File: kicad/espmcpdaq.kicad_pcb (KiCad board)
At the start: 2 copper layers, 151.1 x 149.9 mm, 31 parts, among them J2 Conn_01x15_Female, J3 Conn_01x15_Female

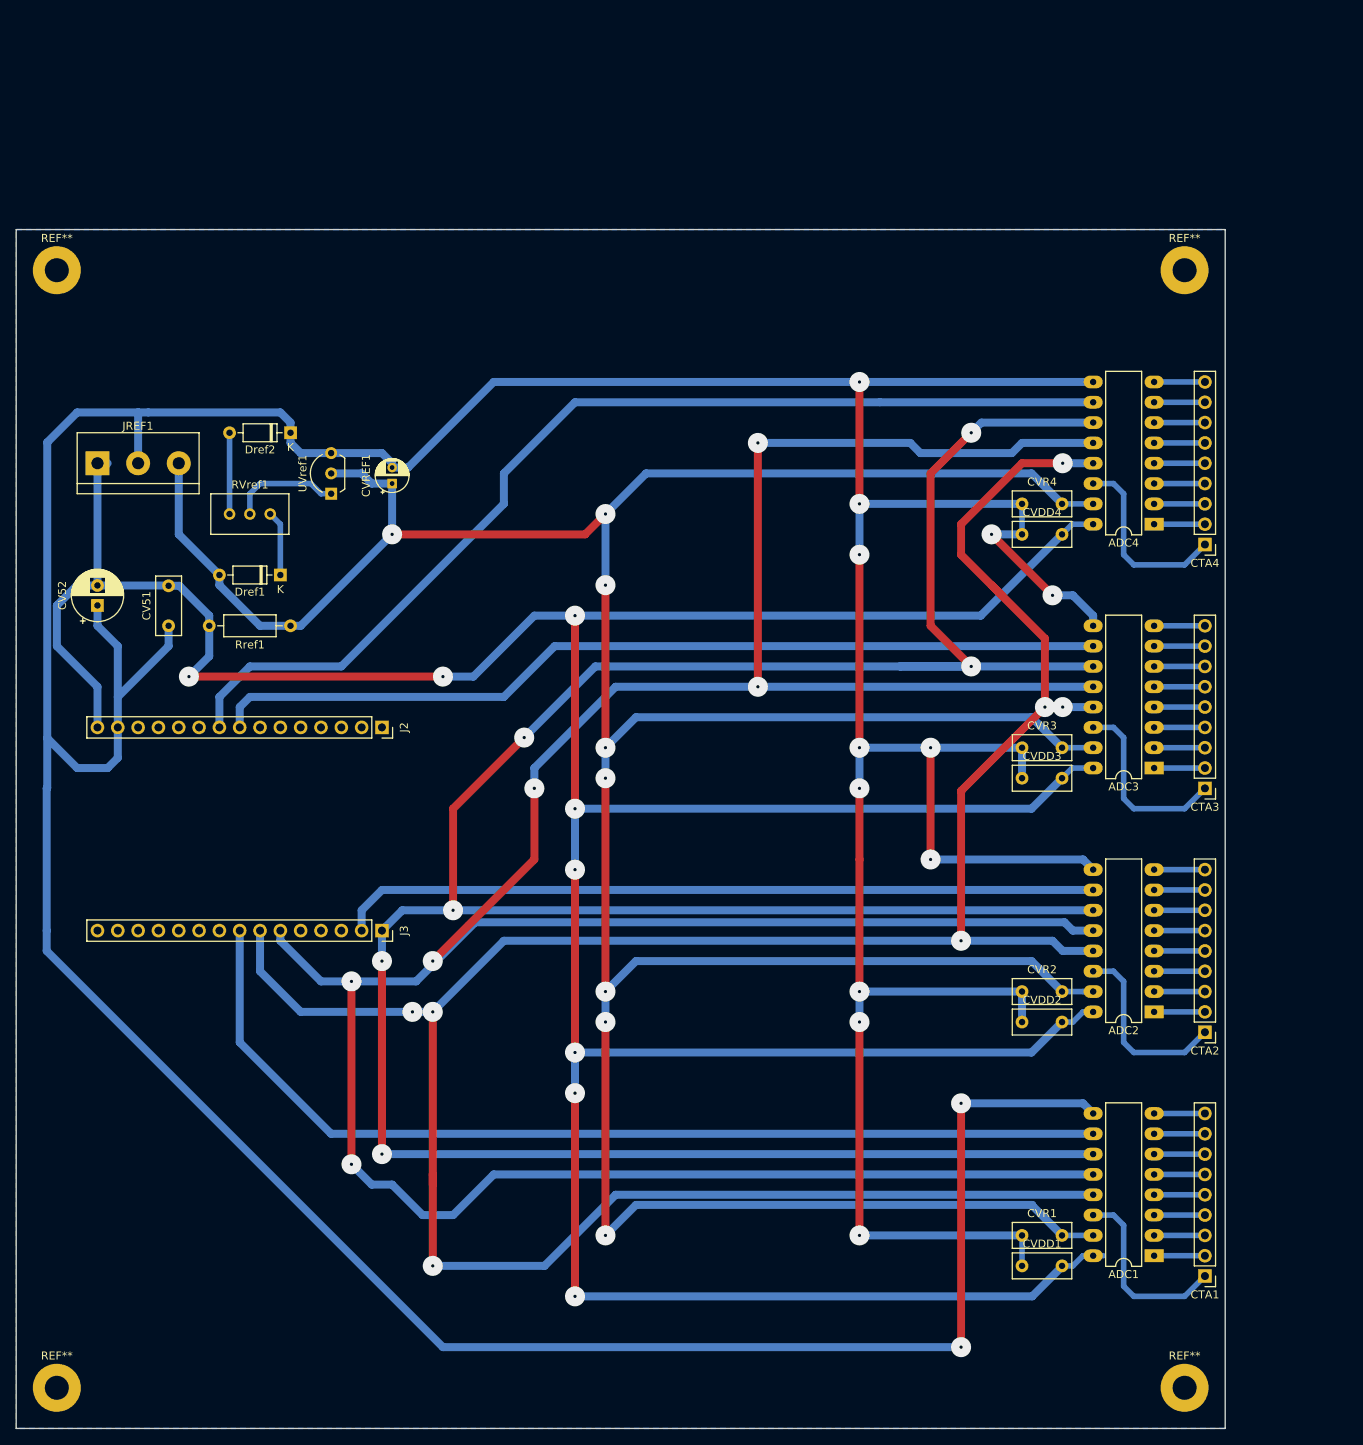
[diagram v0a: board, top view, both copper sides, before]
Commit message: Trying to update to KiCad 8 and changing the board size
The board should have the same size as the multianem8 board
There are several issues with pin compatibility. I should check this
out later...
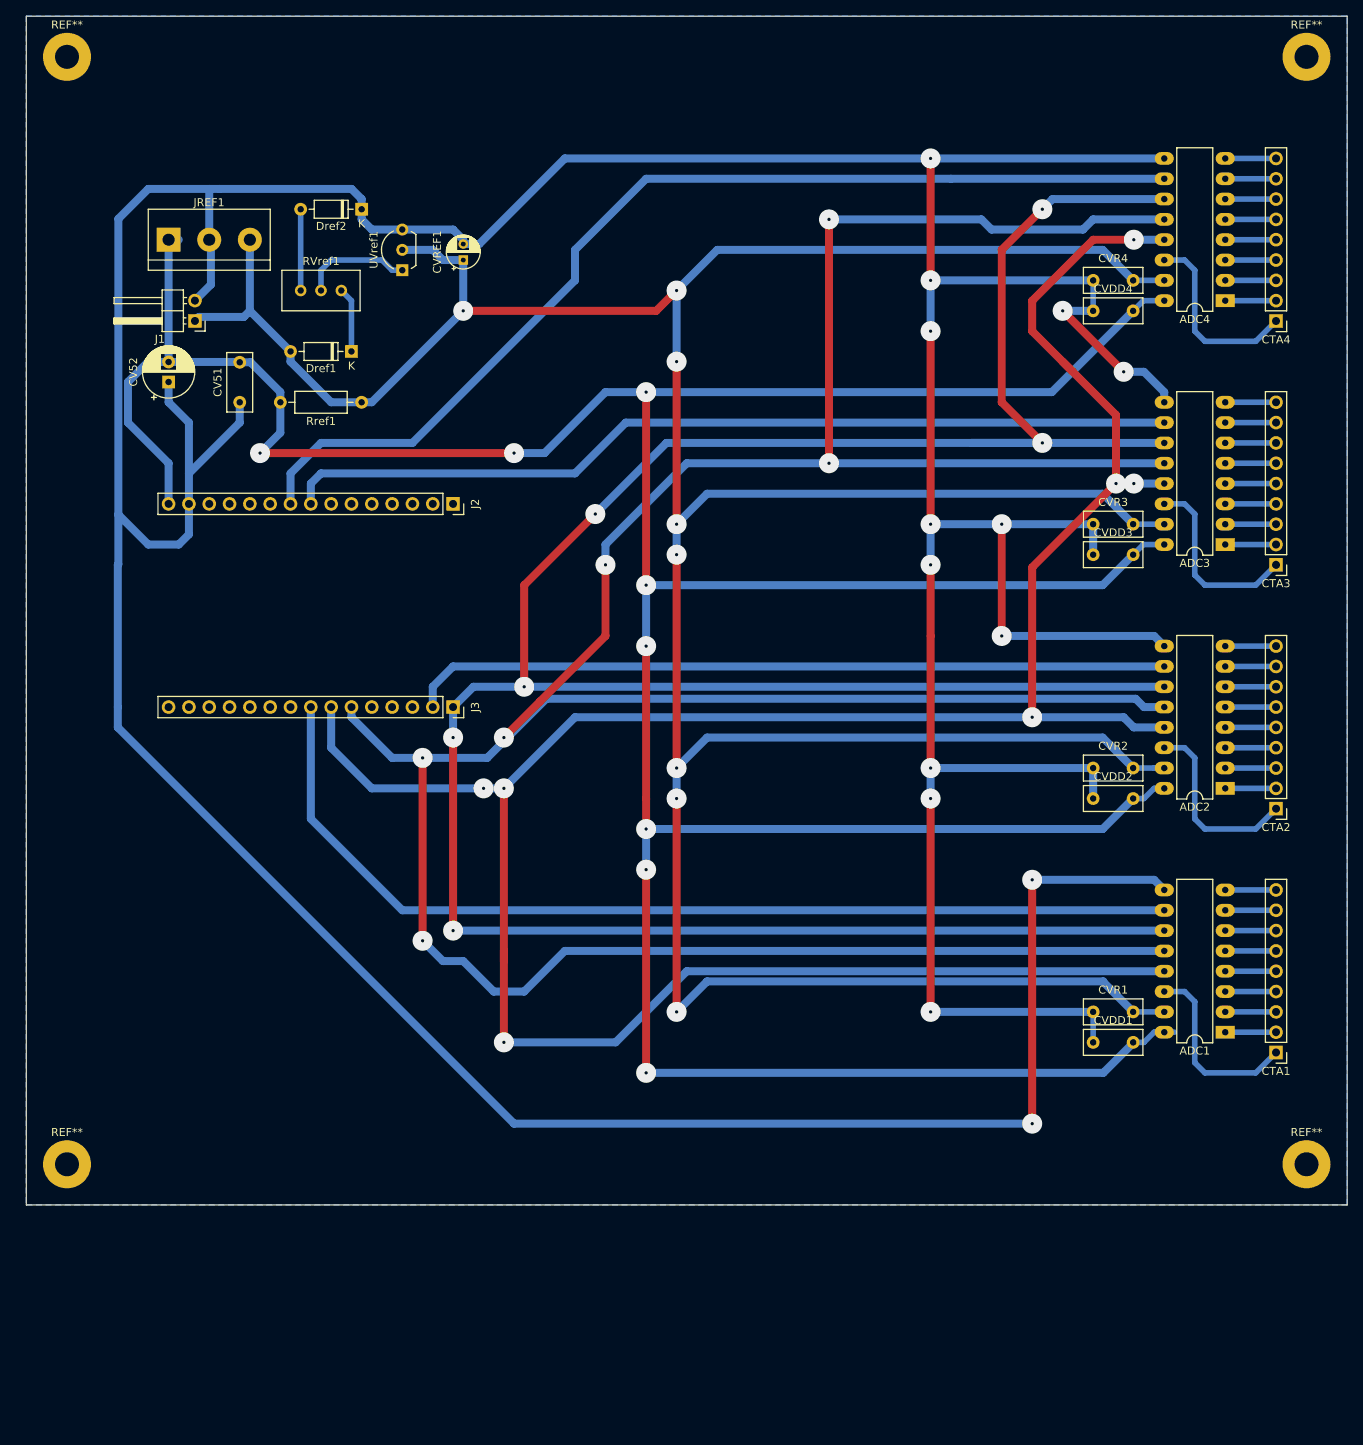
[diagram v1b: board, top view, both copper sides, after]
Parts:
- added J1: Conn_01x02, Connector_PinHeader_2.54mm:PinHeader_1x02_P2.54mm_Horizontal, F.Cu at (41.4, 52.1)
- moved REF** 31.8 mm to (180.3, 157.5)
- moved REF** 30.7 mm to (180.3, 19.1)
- moved ADC2 29.3 mm to (170.2, 110.5)
- moved CTA4 29.3 mm to (176.5, 52.1)
- moved J3 29.3 mm to (73.7, 100.3)
- moved CV51 29.3 mm to (47.0, 62.2)
- moved Dref2 29.3 mm to (62.2, 38.1)
- moved RVref1 29.3 mm to (59.7, 48.3)
- moved Rref1 29.3 mm to (62.2, 62.2)
- moved ADC1 29.3 mm to (170.2, 141.0)
- moved ADC3 29.3 mm to (170.2, 80.0)
- moved ADC4 29.3 mm to (170.2, 49.5)
- moved CTA1 29.3 mm to (176.5, 143.5)
- moved CTA2 29.3 mm to (176.5, 113.0)
- moved CTA3 29.3 mm to (176.5, 82.5)
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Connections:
- J2 pad 1: (no net) -> unconnected-(J2-Pin_1-Pad1)
- J2 pad 10: (no net) -> unconnected-(J2-Pin_10-Pad10)
- J2 pad 11: (no net) -> unconnected-(J2-Pin_11-Pad11)
- J2 pad 12: (no net) -> unconnected-(J2-Pin_12-Pad12)
- J2 pad 13: (no net) -> unconnected-(J2-Pin_13-Pad13)
- J2 pad 2: (no net) -> unconnected-(J2-Pin_2-Pad2)
- J2 pad 3: (no net) -> unconnected-(J2-Pin_3-Pad3)
- J2 pad 4: (no net) -> unconnected-(J2-Pin_4-Pad4)
- J2 pad 5: (no net) -> unconnected-(J2-Pin_5-Pad5)
- J2 pad 6: (no net) -> unconnected-(J2-Pin_6-Pad6)
- J2 pad 7: (no net) -> unconnected-(J2-Pin_7-Pad7)
- J3 pad 10: (no net) -> unconnected-(J3-Pin_10-Pad10)
- J3 pad 11: (no net) -> unconnected-(J3-Pin_11-Pad11)
- J3 pad 12: (no net) -> unconnected-(J3-Pin_12-Pad12)
- J3 pad 13: (no net) -> unconnected-(J3-Pin_13-Pad13)
- J3 pad 14: (no net) -> unconnected-(J3-Pin_14-Pad14)
- J3 pad 15: (no net) -> unconnected-(J3-Pin_15-Pad15)
- J3 pad 3: (no net) -> unconnected-(J3-Pin_3-Pad3)
- J3 pad 4: (no net) -> unconnected-(J3-Pin_4-Pad4)
- J3 pad 5: (no net) -> unconnected-(J3-Pin_5-Pad5)
- J3 pad 9: (no net) -> unconnected-(J3-Pin_9-Pad9)
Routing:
- net GND: track 791.0 -> 799.5 mm
- net /Vref: track 435.2 -> 442.6 mm
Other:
- board size 151.1 x 149.9 mm -> 165.1 x 148.6 mm
- net class Default removed
